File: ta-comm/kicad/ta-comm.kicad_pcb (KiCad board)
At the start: 4 copper layers, 45 x 45 mm, 53 parts, among them IC1 F2972NEGK, IC2 STA0693A, IC3 RFFM6404, IC4 CC1110F32RHHR, J1 A-1JB, J2 Conn_01x04, J3 Conn_01x04, J4 Conn_01x16, J5 Conn_01x16, Y1 FOX924B-27

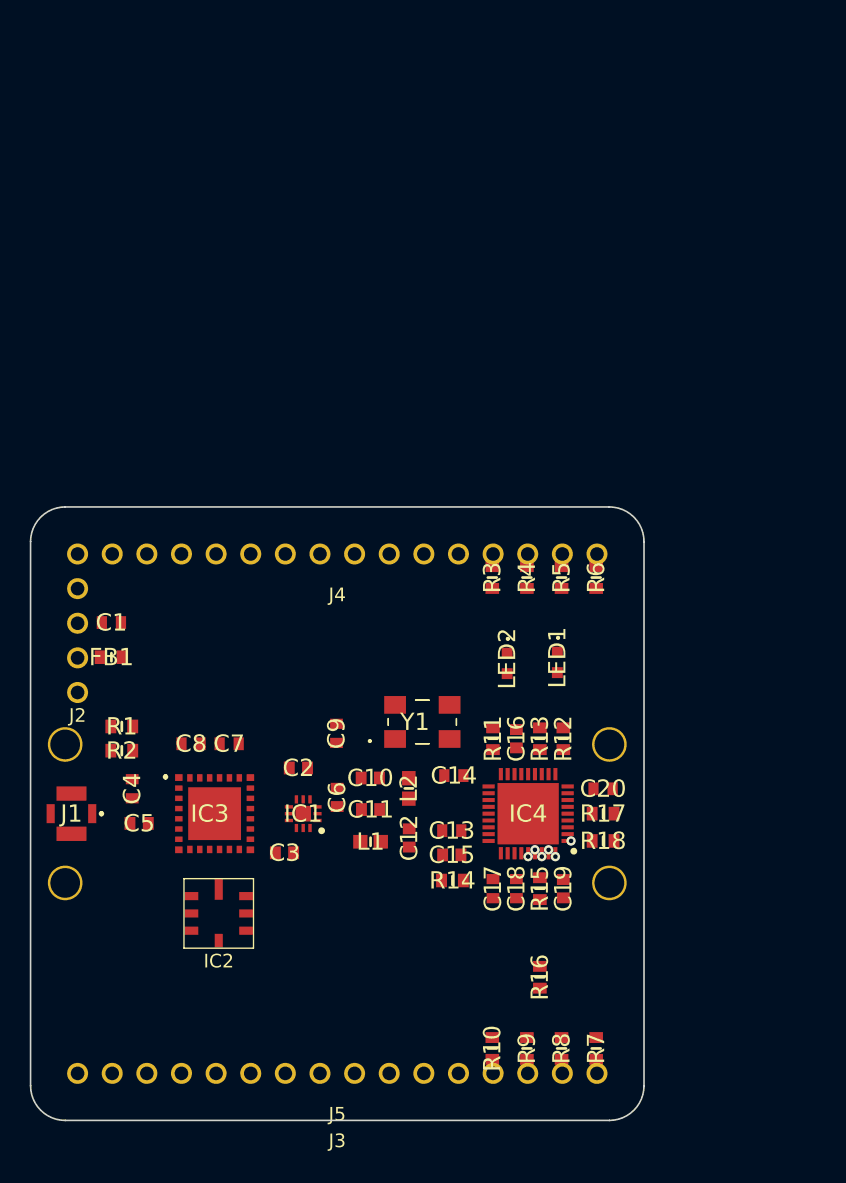
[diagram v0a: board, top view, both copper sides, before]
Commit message: Updates communication board schematic
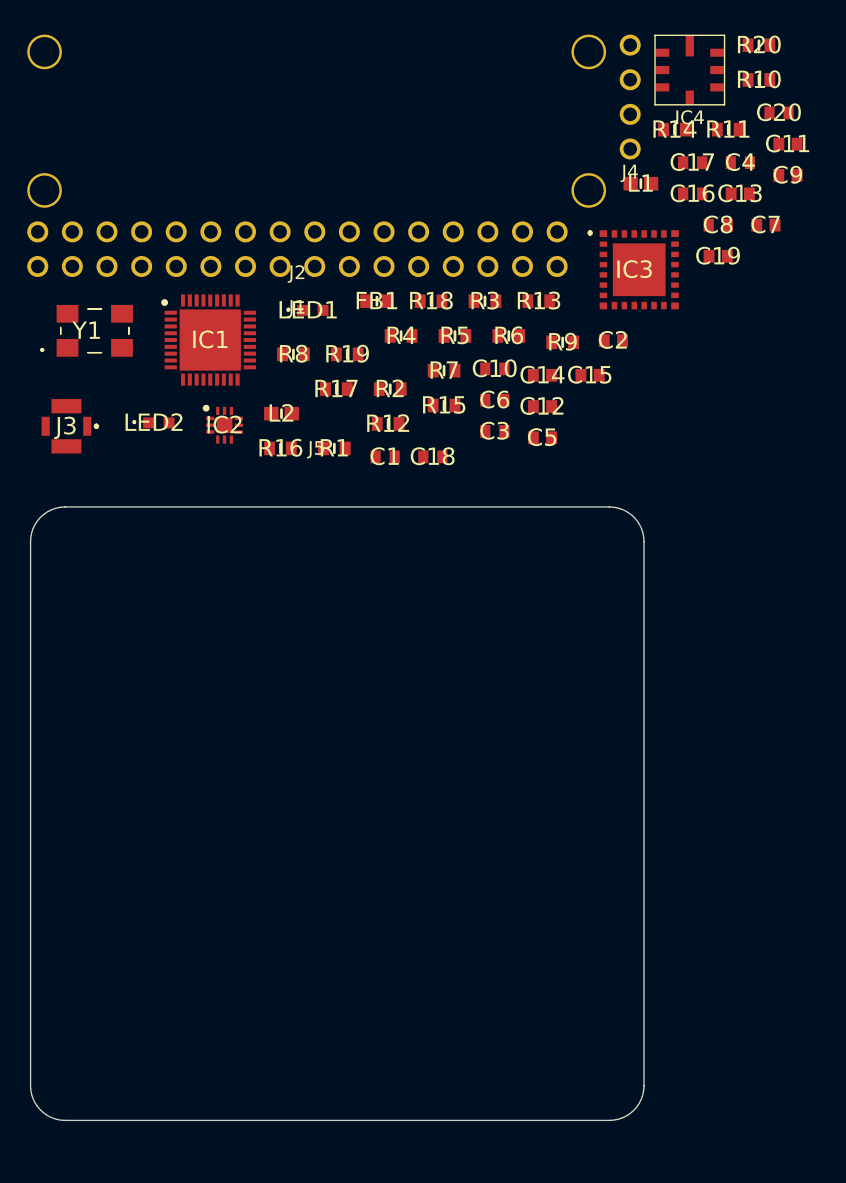
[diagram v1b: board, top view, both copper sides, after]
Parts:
- added R19: MCT06030C6801FP500, ta-comm:RESC1608X55N, F.Cu at (155.7, 74.3)
- added R20: MCT06030C1501FP500, ta-comm:RESC1608X55N, F.Cu at (185.9, 51.6)
- C1: value GRM188R71A225KE15D -> 0603ZC104KAT2A
- C10, C6: value 885012006010 -> 0603ZC104KAT2A; footprint ta-comm:CAPC1608X87N -> ta-comm:CAPC1608X90N
- C12: value VJ0603A3R9BXQCW1BC -> 885012006010
- C13, C14: value 0603ZC104KAT2A -> 885012006010; footprint ta-comm:CAPC1608X90N -> ta-comm:CAPC1608X87N
- C16: value 885012006010 -> GRM188R71A225KE15D; footprint ta-comm:CAPC1608X87N -> ta-comm:CAPC1608X90N
- C17: value 0603ZC104KAT2A -> 0603ZC105KAT2A
- C19: value 885012006014 -> 885012006010
- C2: value 885012006010 -> 885012006014
- C20: value 0603ZC104KAT2A -> CC0603KRX7R6BB224
- C3: value 885012006010 -> 0603ZC105KAT2A; footprint ta-comm:CAPC1608X87N -> ta-comm:CAPC1608X90N
- C4: value CC0603KRX7R6BB224 -> 0603ZC104KAT2A
- C7: value 0603ZC105KAT2A -> 885012006010; footprint ta-comm:CAPC1608X90N -> ta-comm:CAPC1608X87N
- C8: value 0603ZC105KAT2A -> 0603ZC104KAT2A
- C9: value 0603ZC104KAT2A -> VJ0603A3R9BXQCW1BC; footprint ta-comm:CAPC1608X90N -> ta-comm:CAPC1608X87N
- IC1: value F2972NEGK -> CC1110F32RHHR; footprint ta-comm:QFN50P200X200X55-13N-D -> ta-comm:QFN50P600X600X100-37N-D
- IC2: value STA0693A -> F2972NEGK; footprint ta-comm:STA0693A -> ta-comm:QFN50P200X200X55-13N-D
- IC4: value CC1110F32RHHR -> STA0693A; footprint ta-comm:QFN50P600X600X100-37N-D -> ta-comm:STA0693A
- J1: value A-1JB -> Conn_01x16; footprint ta-comm:A1JB -> ta-comm:PinSocket_1x16_TartanArtibeus
- J2: value Conn_01x04 -> Conn_01x16; footprint ta-comm:PinSocket_1x4_TartanArtibeus -> ta-comm:PinSocket_1x16_TartanArtibeus
- J3: value Conn_01x04 -> A-1JB; footprint ta-comm:MountingHoles_TartanArtibeus -> ta-comm:A1JB
- J4: value Conn_01x16 -> Conn_01x04; footprint ta-comm:PinSocket_1x16_TartanArtibeus -> ta-comm:PinSocket_1x4_TartanArtibeus
- J5: value Conn_01x16 -> Conn_01x04; footprint ta-comm:PinSocket_1x16_TartanArtibeus -> ta-comm:MountingHoles_TartanArtibeus
- R1: value MCT06030C1501FP500 -> MCT06030C1001FP500
- R10: value MCT06030C1000FP500 -> MCT06030C5602FP500
- R12, R13, R15, R17, R18: value MCT06030C1001FP500 -> MCT06030C1000FP500
- R14: value MCT06030C5602FP500 -> MCT06030C1000FP500
- R16: value MCT06030C3302FP500 -> MCT06030C1000FP500
- R2: value MCT06030C6801FP500 -> MCT06030C1001FP500
- R3, R4, R5, R6, R7: value MCT06030C1000FP500 -> MCT06030C1001FP500
- R8: value MCT06030C1000FP500 -> MCT06030C3302FP500
- moved R10 73.7 mm to (185.9, 54.2), turned to 0 degrees
- moved J5 69.9 mm to (153.5, 57.2)
- moved C4 64.0 mm to (184.6, 60.2), turned to 0 degrees
- moved C11 57.6 mm to (188.1, 58.9), turned to 0 degrees
- moved R14 57.4 mm to (179.7, 57.8), turned to 0 degrees
- moved IC4 55.8 mm to (180.9, 53.5), turned to 0 degrees
- moved C17 55.2 mm to (181.1, 60.2), turned to 0 degrees
- moved C7 54.8 mm to (186.4, 64.8)
- moved R8 54.6 mm to (151.8, 74.3), turned to 0 degrees
- moved C8 54.3 mm to (182.9, 64.8), turned to 0 degrees
- moved C9 52.7 mm to (188.1, 61.2), turned to 0 degrees
- moved L1 52.2 mm to (177.3, 61.8), turned to 0 degrees
- moved R9 51.9 mm to (171.5, 73.4), turned to 0 degrees
- moved C13 51.3 mm to (184.6, 62.5), turned to 0 degrees
- moved C20 51.2 mm to (187.4, 56.6), turned to 0 degrees
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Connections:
- C13 pad 1: /VDD_FILT -> Net-(C11-Pad2)
- C13 pad 2: GND -> Net-(C13-Pad2)
- C14 pad 1: /VDD_FILT -> Net-(C14-Pad1)
- C14 pad 2: GND -> Net-(C14-Pad2)
- C15 pad 1: /VDD_FILT -> Net-(C15-Pad1)
- C15 pad 2: GND -> Net-(C15-Pad2)
- C18 pad 1: Net-(C18-Pad1) -> /VDD_FILT
- C19 pad 2: GND -> Net-(C19-Pad2)
- C2 pad 2: Net-(C2-Pad2) -> GND
- C20 pad 1: /VDD_FILT -> Net-(C20-Pad1)
- C3 pad 2: Net-(C3-Pad2) -> GND
- C5 pad 2: Net-(C5-Pad2) -> GND
- C6 pad 1: Net-(C11-Pad2) -> Net-(C6-Pad1)
- C6 pad 2: Net-(C6-Pad2) -> GND
- C7 pad 1: /VDD_FILT -> Net-(C7-Pad1)
- C9 pad 1: /VDD_FILT -> Net-(C11-Pad1)
- IC1 pad 1: GND -> /CTS0
- IC1 pad 10: GND -> /VDD_FILT
- IC1 pad 11: Net-(C3-Pad1) -> /RX1
- IC1 pad 12: GND -> /LED1
- IC1 pad 13: GND -> /LED2
- IC1 pad 2: Net-(C6-Pad2) -> /VDD_FILT
- IC1 pad 3: GND -> /RF_BYP
- IC1 pad 4: GND -> /RF_EN
- IC1 pad 5: Net-(C2-Pad1) -> Net-(IC1-Pad5)
- IC1 pad 6: GND -> Net-(IC1-Pad6)
- IC1 pad 7: /N_RX_MODE -> /CTS1
- IC1 pad 8: Net-(IC1-Pad8) -> /RTS1
- IC1 pad 9: /VDD_FILT -> /TX1
- IC2 pad 2: Net-(IC2-Pad2) -> Net-(C13-Pad2)
- IC2 pad 5: GND -> Net-(C14-Pad1)
- IC2 pad 6: Net-(IC2-Pad6) -> GND
- IC2 pad 7: GND -> /N_RX_MODE
- IC2 pad 8: GND -> Net-(IC2-Pad8)
- IC3 pad 10: Net-(IC2-Pad2) -> Net-(IC3-Pad10)
- IC3 pad 13: Net-(IC2-Pad6) -> Net-(IC3-Pad13)
- IC3 pad 18: Net-(C2-Pad2) -> Net-(C14-Pad2)
- IC3 pad 20: Net-(C3-Pad2) -> Net-(C15-Pad2)
- IC3 pad 5: Net-(C4-Pad1) -> Net-(C20-Pad1)
- IC3 pad 7: Net-(C5-Pad1) -> Net-(C19-Pad1)
- IC4 pad 1: /CTS0 -> GND
- IC4 pad 2: /VDD_FILT -> Net-(IC3-Pad10)
- IC4 pad 3: /RF_BYP -> GND
- IC4 pad 4: /RF_EN -> GND
- IC4 pad 5: Net-(IC4-Pad5) -> GND
- IC4 pad 6: Net-(IC4-Pad6) -> Net-(IC3-Pad13)
- IC4 pad 7: /CTS1 -> GND
- IC4 pad 8: /RTS1 -> GND
- J1 pad 1: Net-(C5-Pad2) -> Net-(J1-Pad1)
- J1 pad 2: GND -> Net-(J1-Pad2)
- J1 pad 4: GND -> Net-(J1-Pad4)
- J2 pad 1: VDD -> Net-(J2-Pad1)
- J2 pad 2: GND -> Net-(J2-Pad2)
- J2 pad 3: /PDIO -> GND
- J2 pad 4: /PCLK -> /D0
- J3 pad 1: GND -> Net-(C19-Pad2)
- J4 pad 1: Net-(J4-Pad1) -> VDD
- J4 pad 2: Net-(J4-Pad2) -> GND
- J4 pad 3: GND -> /PDIO
- J4 pad 4: Net-(J4-Pad4) -> /PCLK
- J5 pad 1: Net-(J5-Pad1) -> GND
- J5 pad 2: Net-(J5-Pad2) -> GND
- J5 pad 4: /D0 -> GND
- L1 pad 1: Net-(C12-Pad1) -> Net-(IC1-Pad23)
- L1 pad 2: Net-(C11-Pad2) -> Net-(C12-Pad1)
- L2 pad 1: Net-(C11-Pad1) -> Net-(IC1-Pad23)
- L2 pad 2: Net-(C10-Pad1) -> Net-(C11-Pad2)
- R1 pad 1: /VDD_FILT -> /RF_BYP
- R1 pad 2: Net-(C4-Pad1) -> GND
- R10 pad 1: /RTS0 -> Net-(IC1-Pad27)
- R10 pad 2: Net-(J5-Pad13) -> GND
- R11 pad 1: Net-(IC4-Pad21) -> /RTS1
- R11 pad 2: Net-(R11-Pad2) -> Net-(J1-Pad13)
- R12 pad 1: /LED1 -> /CTS1
- R12 pad 2: Net-(LED1-Pad2) -> Net-(J1-Pad14)
- R13 pad 1: /LED2 -> /RX1
- R13 pad 2: Net-(LED2-Pad2) -> Net-(J1-Pad15)
- R14 pad 1: Net-(IC4-Pad27) -> /TX1
- R14 pad 2: GND -> Net-(J1-Pad16)
- R15 pad 1: Net-(C19-Pad1) -> /TX1
- R15 pad 2: /D0 -> Net-(J2-Pad16)
- R16 pad 1: /D0 -> /RX1
- R16 pad 2: /VDD_FILT -> Net-(J2-Pad15)
- R17 pad 1: /VDD_FILT -> /CTS1
- R17 pad 2: /RF_EN -> Net-(J2-Pad14)
- R18 pad 1: /RF_BYP -> /RTS1
- R18 pad 2: GND -> Net-(J2-Pad13)
- R2 pad 1: Net-(C4-Pad1) -> /RF_EN
- R2 pad 2: GND -> /VDD_FILT
- R3 pad 1: /RTS1 -> /LED1
- R3 pad 2: Net-(J4-Pad13) -> Net-(LED1-Pad2)
- R4 pad 1: /CTS1 -> /LED2
- R4 pad 2: Net-(J4-Pad14) -> Net-(LED2-Pad2)
- R5 pad 1: /RX1 -> /N_RX_MODE
- R5 pad 2: Net-(J4-Pad15) -> /VDD_FILT
- R6 pad 1: /TX1 -> /TX_MODE
- R6 pad 2: Net-(J4-Pad16) -> GND
- R7 pad 1: /TX0 -> Net-(C2-Pad1)
- R7 pad 2: Net-(J5-Pad16) -> /D0
- R8 pad 1: /RX0 -> /D0
- R8 pad 2: Net-(J5-Pad15) -> /VDD_FILT
- R9 pad 1: /CTS0 -> Net-(IC1-Pad21)
- R9 pad 2: Net-(J5-Pad14) -> Net-(R9-Pad2)
- Y1 pad 3: Net-(R11-Pad2) -> Net-(R9-Pad2)
- Y1 pad 4: /VDD_FILT -> Net-(C10-Pad1)
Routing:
- net /TX_MODE: vias 1 -> 0
- net /TX0: vias 1 -> 0
- net /RX0: vias 1 -> 0
- net /RTS0: vias 1 -> 0
- net /N_RX_MODE: vias 1 -> 0
- net /CTS0: vias 1 -> 0

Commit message: Updates communication board PCB
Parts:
- moved IC4 65.9 mm to (163.4, 117.0)
- moved R10 64.4 mm to (146.8, 105.3)
- moved J2 61.8 mm to (155.0, 127.0)
- moved C4 58.8 mm to (143.9, 102.7), turned to 90 degrees
- moved C8 58.3 mm to (146.8, 110.5)
- moved C9 58.1 mm to (150.5, 105.5), turned to 90 degrees
- moved C7 58.0 mm to (146.7, 107.1)
- moved C11 57.6 mm to (153.1, 104.6)
- moved J4 56.9 mm to (135.9, 95.3)
- moved L1 54.9 mm to (150.6, 109.7), turned to 270 degrees
- moved C16 54.8 mm to (138.7, 97.4), turned to 180 degrees
- moved C13 54.3 mm to (153.1, 106.8)
- moved R20 53.8 mm to (167.4, 102.2)
- moved R18 53.7 mm to (166.4, 123.9), turned to 270 degrees
- moved J5 50.8 mm to (155.0, 108.0)
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
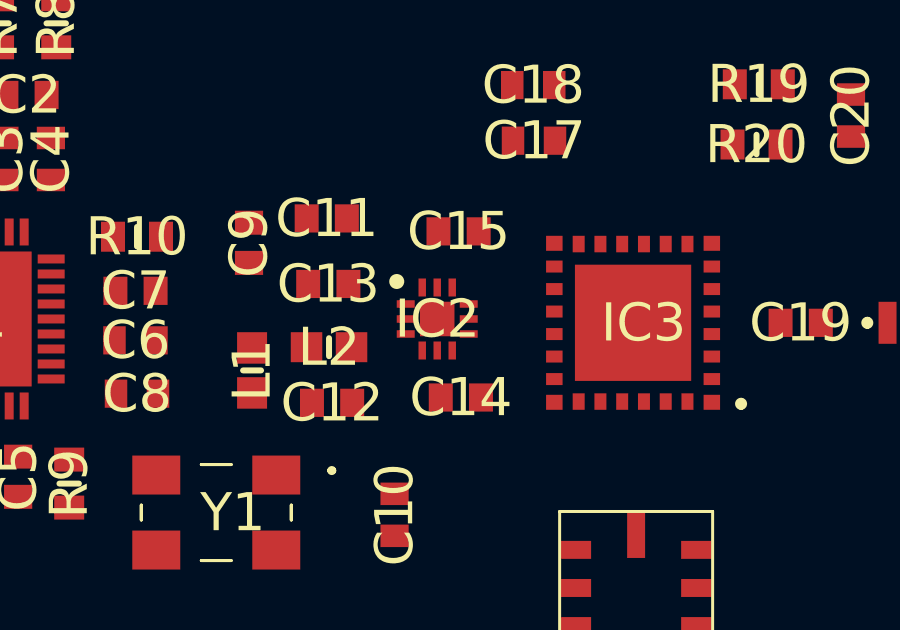
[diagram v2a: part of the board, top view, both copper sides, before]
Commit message: Updates communication board schematic and PCB
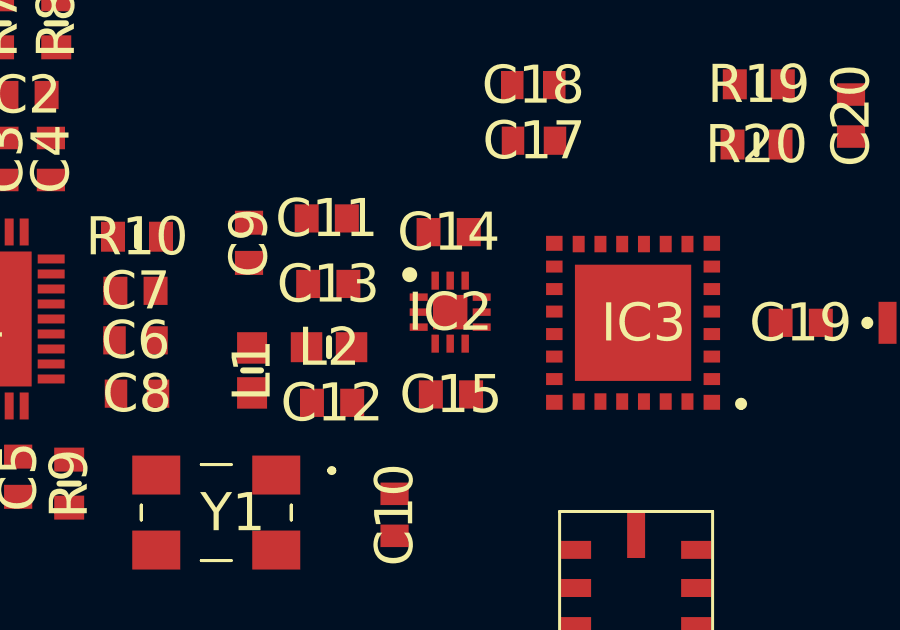
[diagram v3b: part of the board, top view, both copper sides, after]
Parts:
- IC2: footprint ta-comm:QFN50P200X200X55-13N-D -> QFN50P200X200X55-13N-D
- moved C14 5.53 mm to (157.1, 105.1)
- moved C15 5.44 mm to (157.2, 110.5)
- moved IC2 0.49 mm to (157.2, 107.8)
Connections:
- net /N_RX_MODE renamed /RX_MODE
- IC2 pad 11: Net-(C15-Pad1) -> Net-(C14-Pad1)
- IC2 pad 5: Net-(C14-Pad1) -> Net-(C15-Pad1)
- R11 pad 1: /RTS1 -> /RTS0
- R12 pad 1: /CTS1 -> /CTS0
- R13 pad 1: /RX1 -> /RX0
- R14 pad 1: /TX1 -> /TX0
- R5 pad 2: /VDD_FILT -> GND

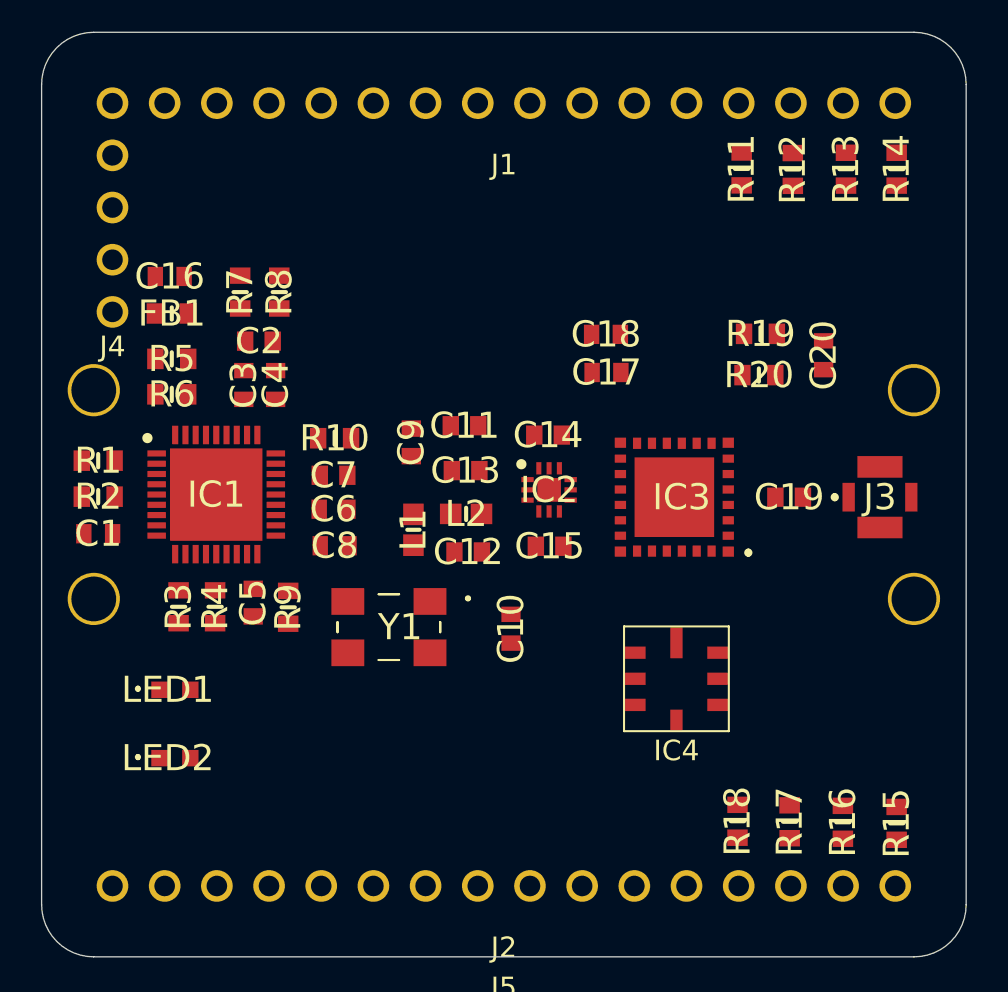
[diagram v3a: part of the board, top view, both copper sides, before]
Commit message: Updates communication board PCB component positions
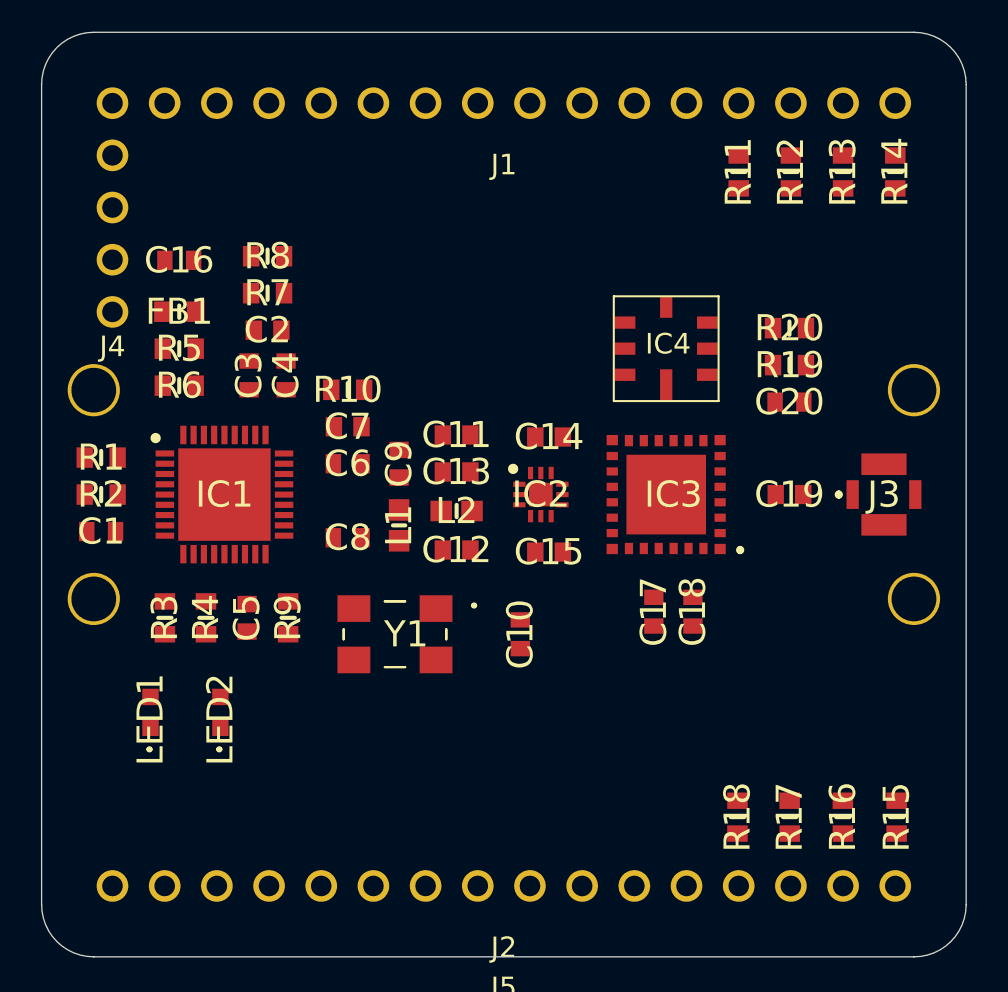
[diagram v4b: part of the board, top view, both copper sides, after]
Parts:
- moved IC4 16.1 mm to (162.9, 100.9), turned to 180 degrees
- moved C18 14.1 mm to (164.2, 113.7), turned to 270 degrees
- moved C17 11.9 mm to (162.3, 113.7), turned to 270 degrees
- moved LED2 3.14 mm to (141.2, 118.6), turned to 90 degrees
- moved C20 2.82 mm to (168.9, 103.5), turned to 0 degrees
- moved R20 2.73 mm to (168.9, 99.9), turned to 180 degrees
- moved C7 2.46 mm to (147.4, 104.7)
- moved R10 2.44 mm to (147.4, 102.9)
- moved C6 2.32 mm to (147.4, 106.5)
- moved R19 2.08 mm to (168.9, 101.7)
- moved R8 1.84 mm to (143.5, 96.4), turned to 180 degrees
- moved LED1 1.62 mm to (137.8, 118.6), turned to 90 degrees
- moved R7 1.34 mm to (143.5, 98.2), turned to 0 degrees
- moved C9 1.20 mm to (149.9, 106.5)
- moved C16 0.91 mm to (139.2, 96.6)
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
